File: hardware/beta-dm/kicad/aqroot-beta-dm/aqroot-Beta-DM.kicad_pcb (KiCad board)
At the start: 4 copper layers, 74 x 155 mm, 188 parts, among them J1 CH280QV10-CT_50P, J2 Molex_5025700893, J3 USB_C_Receptacle_USB2.0_16P, J4 JST-PH-2 BATTERY, J5 COMMUNITY_HEADER_2x13, J6 JST-PH-2 SPEAKER, Q1 AO3400A, SW1 BOOT, SW2 UP, SW3 DOWN, SW4 LEFT, SW5 RIGHT, SW6 A_SELECT, SW7 B_BACK, SW8 HOME, SW9 SW_SPDT, U1 ESP32-S3-WROOM-1, U10 USBLC6-2SC6, U11 BQ25185, U12 TPS63020, U13 TPS61023, U14 MAX17048, U15 TPS22918, U16 TCA9517ADGK, U17 TPS61169DCKR, U2 TCA9535PWR, U3 TCA9535PWR, U4 BMI270, U5 MAX98357A, U6 TSOP38238, U7 E07-400M10S, U8 E22-900M22S, U9 ST25R3916-AQET

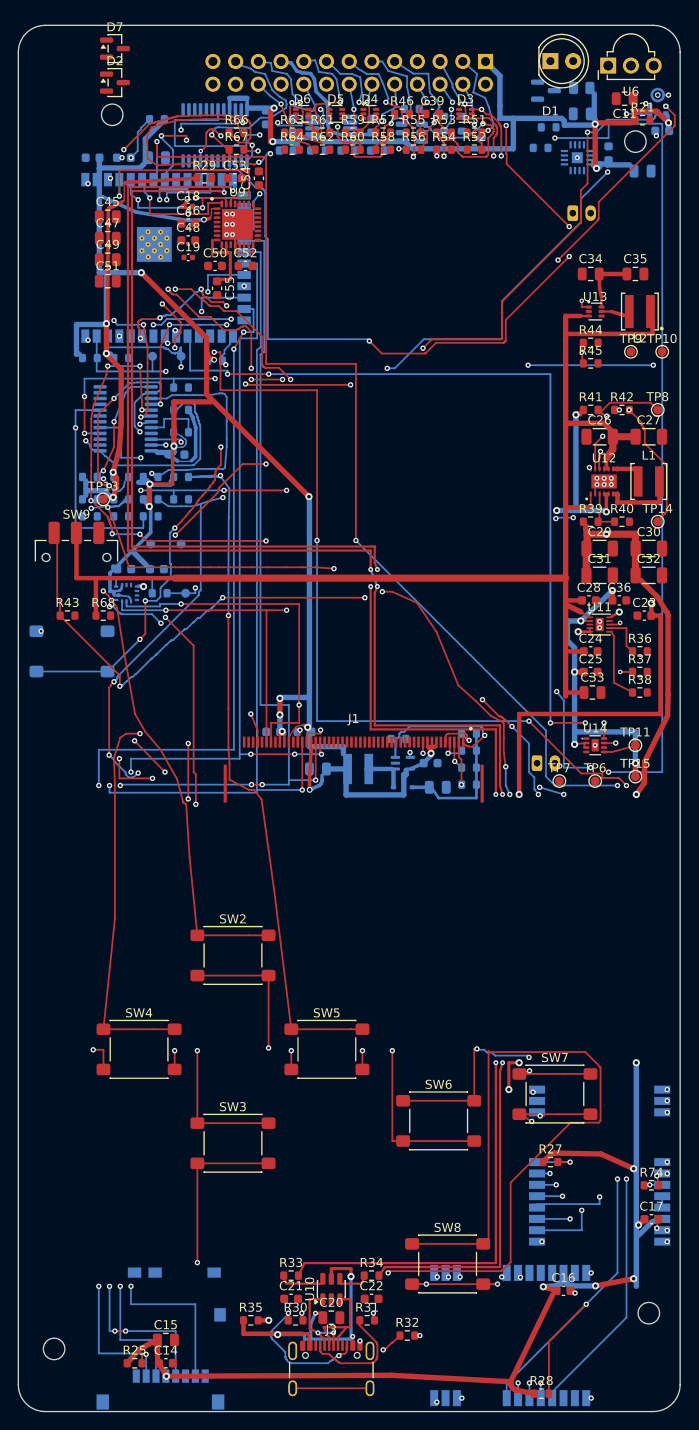
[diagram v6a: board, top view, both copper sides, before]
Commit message: Beta-DM: GND closeout — stitch 76 of 91 fitted ground islands
Reclassify all 130 GND ratsnest lines: 100 fitted must-ground, 30 DNP-only,
0 already-satisfied, 0 special. Work is planned per island, not per rat:
91 isolated fitted islands owe copper, 35 DNP-only islands owe nothing and
were deliberately left alone.

Land 134 segments and 55 vias in three writes. Nothing removed, nothing
changed — signal copper modifications are zero. Every stitch is
pad -> stub -> local via -> In1, and every via clears the obstacle model,
the RF keepouts, the In1 zone outline, a 0.125 mm solder-mask web to every
paste aperture on every net, and 0.250 mm hole-to-hole against every hole
on the board.

Result: GND 130 -> 52, total unconnected 215 -> 137. DRC 0 errors,
0 new warnings, 0 parity issues. Worst mask web 0.1250 mm, worst
hole-to-hole 0.4818 mm, no via under a solder termination.

Ledger: 137 = A63 + B1(15) + B2(37) + C0 + D22.

15 fitted islands remain open. Three independent passes converged on the
same set and the most permissive one closed 0 of 15: these pads escape into
narrow channels where a via's 0.575 mm halo does not fit. They are the
fine-pitch pockets around U2, U3, U4 and J3 and the passives in them, and
they are pour-resolvable rather than via-resolvable. Deferred to the pour
pass as the ruling directs.

Three corrections:
- the router did not enforce hole-to-hole against same-net holes, and
  generated a C5/2 via whose drill would break out into an existing GND
  via 0.050 mm away. KiCad only warns on same-net hole-to-hole, so the
  error gate would not have caught it. Model corrected; C5/2 re-routed as
  a pad-to-pad join needing no via.
- a 210 mm 10-via "stitch" was generated and rejected; stitches are now
  capped at 6 mm.
- fab note 3b claimed the XGPIO5 via was the smallest on the board. It was
  not — four 0.50/0.25 vias already existed. Corrected to name the
  0.125 mm mask web, which is genuinely unique, as the critical attribute.

No pours, no E6 retir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
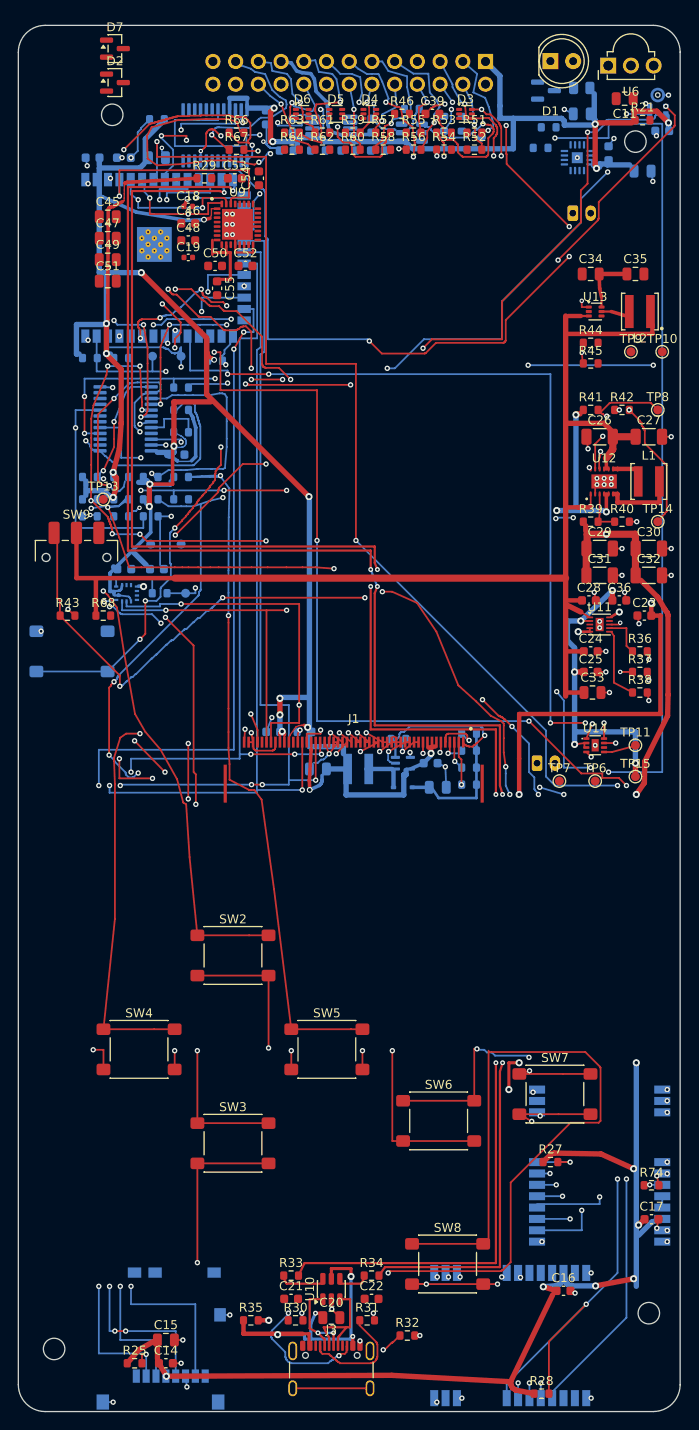
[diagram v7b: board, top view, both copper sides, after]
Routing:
- net GND: track 112.4 -> 216.5 mm, vias 61 -> 116
